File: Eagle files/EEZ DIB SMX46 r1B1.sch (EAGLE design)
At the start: 156 parts, among them IC1 STM32F030C6T6, IC2 74HC1G126DBVT, IC3 M24C32-WMN6P, IC4 LP2985-33DBVR, IC5 74HC2G04GW,125, K1 FTR-C1GA012G-B05, K10 FTR-C1GA012G-B05, K11 FTR-C1GA012G-B05, K12 FTR-C1GA012G-B05, K13 FTR-C1GA012G-B05, K14 FTR-C1GA012G-B05, K15 FTR-C1GA012G-B05, K16 FTR-C1GA012G-B05, K17 FTR-C1GA012G-B05, K18 FTR-C1GA012G-B05, K19 FTR-C1GA012G-B05, K2 FTR-C1GA012G-B05, K20 FTR-C1GA012G-B05, K21 FTR-C1GA012G-B05, K22 FTR-C1GA012G-B05, K23 FTR-C1GA012G-B05, K24 FTR-C1GA012G-B05, K3 FTR-C1GA012G-B05, K4 FTR-C1GA012G-B05, K5 FTR-C1GA012G-B05, K6 FTR-C1GA012G-B05, K7 FTR-C1GA012G-B05, K8 FTR-C1GA012G-B05, K9 FTR-C1GA012G-B05, Q1 2N7002, Q10 2N7002, Q11 2N7002, Q12 2N7002, Q13 2N7002, Q14 2N7002, Q15 2N7002, Q16 2N7002, Q17 2N7002, Q18 2N7002, Q19 2N7002, Q2 2N7002, Q20 2N7002, Q21 2N7002, Q22 2N7002, Q23 2N7002, Q24 2N7002, Q25 2N7002, Q3 2N7002, Q4 2N7002, Q5 2N7002, Q6 2N7002, Q7 2N7002, Q8 2N7002, Q9 2N7002, X1 N.C., X2 77317-104-28LF, X3 691327310016, X4 691327310016

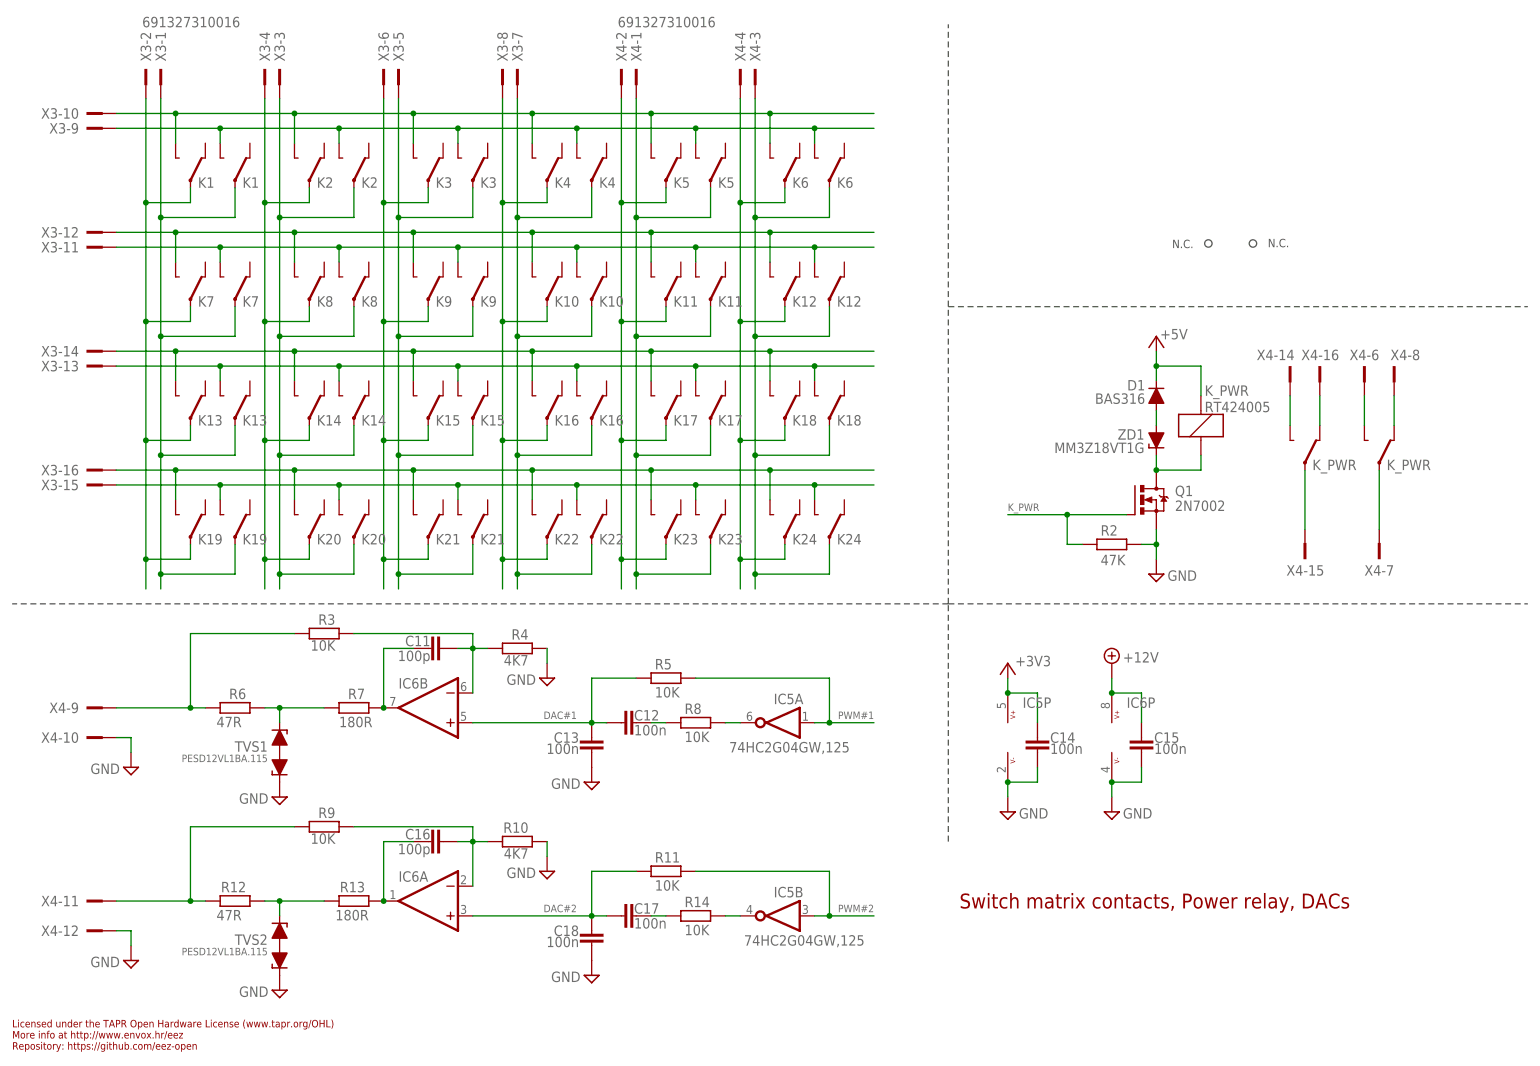
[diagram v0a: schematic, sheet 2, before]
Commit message: UART relocated
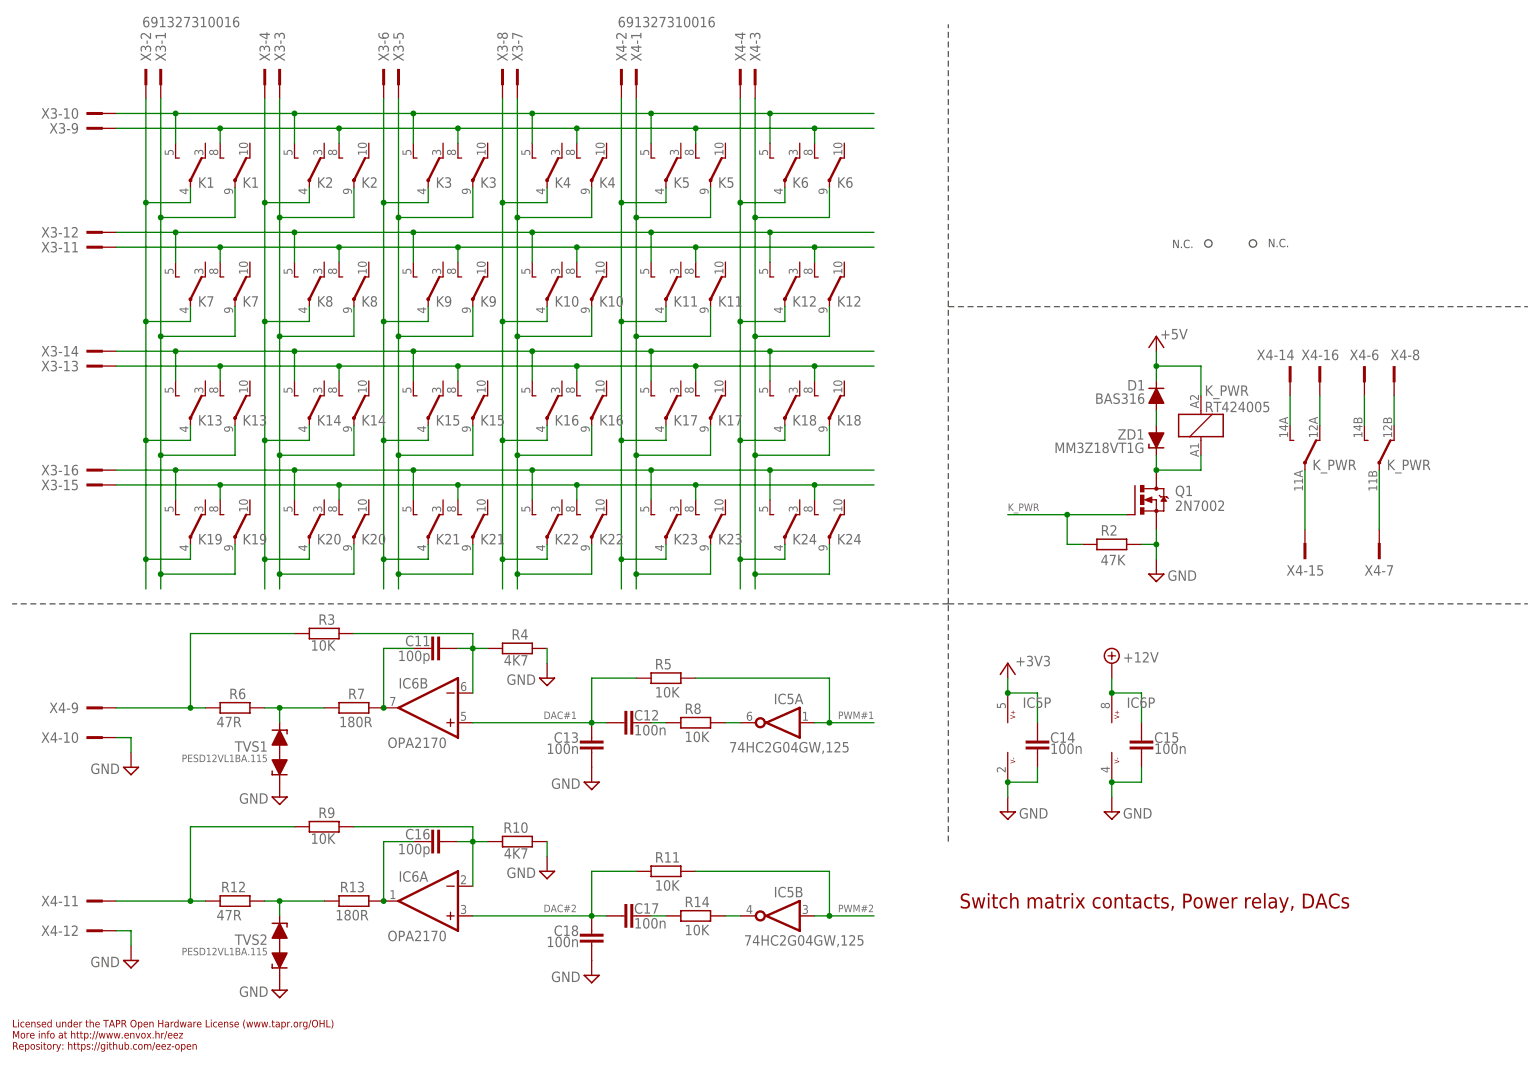
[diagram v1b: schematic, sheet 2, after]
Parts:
- IC6: value (none) -> OPA2170
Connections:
- net K_PWR: now also IC1.PA15; no longer IC1.PA8
- net PWM#1: now also IC1.PA8; no longer IC1.PA10
- net UART_RX: now also IC1.PA10; no longer IC1.PA15
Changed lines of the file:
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@@
 <part name="SUPPLY36" library="supply2" deviceset="GND" device=""/>
 <part name="+3V8" library="supply1" deviceset="+3V3" device=""/>
-<part name="IC6" library="EEZ_Lib1" deviceset="TL072" device="SOIC8"/>
+<part name="IC6" library="EEZ_Lib1" deviceset="TL072" device="SOIC8" value="OPA2170"/>
 <part name="R3" library="rcl" deviceset="R-EU_" device="R0805" value="10K"/>
 <part name="R4" library="rcl" deviceset="R-EU_" device="R0805" value="4K7"/>
@@
 <net name="K_PWR" class="0">
 <segment>
-<pinref part="IC1" gate="G$1" pin="PA8"/>
-<wire x1="241.3" y1="99.06" x2="251.46" y2="99.06" width="0.1524" layer="91"/>
-<label x="243.84" y="99.695" size="1.27" layer="102"/>
+<label x="222.885" y="132.08" size="1.27" layer="102" rot="R90"/>
+<pinref part="IC1" gate="G$1" pin="PA15"/>
+<wire x1="223.52" y1="129.54" x2="223.52" y2="139.7" width="0.1524" layer="91"/>
 </segment>
 </net>
@@
 <net name="PWM#1" class="0">
 <segment>
-<pinref part="IC1" gate="G$1" pin="PA10"/>
-<wire x1="241.3" y1="104.14" x2="251.46" y2="104.14" width="0.1524" layer="91"/>
-<label x="243.84" y="104.775" size="1.27" layer="102"/>
+<label x="243.84" y="99.695" size="1.27" layer="102"/>
+<pinref part="IC1" gate="G$1" pin="PA8"/>
+<wire x1="241.3" y1="99.06" x2="251.46" y2="99.06" width="0.1524" layer="91"/>
 </segment>
 </net>
@@
 <net name="UART_RX" class="0">
 <segment>
-<pinref part="IC1" gate="G$1" pin="PA15"/>
-<wire x1="223.52" y1="129.54" x2="223.52" y2="142.24" width="0.1524" layer="91"/>
-<label x="222.885" y="132.08" size="1.27" layer="102" rot="R90"/>
+<label x="243.84" y="104.775" size="1.27" layer="102"/>
+<wire x1="241.3" y1="104.14" x2="251.46" y2="104.14" width="0.1524" layer="91"/>
+<pinref part="IC1" gate="G$1" pin="PA10"/>
 </segment>
 <segment>
@@
 <segment>
 <pinref part="IC1" gate="G$1" pin="PA14"/>
-<wire x1="226.06" y1="129.54" x2="226.06" y2="142.24" width="0.1524" layer="91"/>
+<wire x1="226.06" y1="129.54" x2="226.06" y2="139.7" width="0.1524" layer="91"/>
 <label x="225.425" y="132.08" size="1.27" layer="102" rot="R90"/>
 </segment>
@@
 <instance part="IC6" gate="B" x="73.66" y="60.96" smashed="yes" rot="R180">
 <attribute name="NAME" x="73.66" y="66.04" size="1.778" layer="95" rot="R180"/>
-<attribute name="VALUE" x="78.74" y="52.07" size="1.778" layer="96" rot="R180"/>
+<attribute name="VALUE" x="76.835" y="55.88" size="1.778" layer="96" rot="R180"/>
 </instance>
 <instance part="C11" gate="G$1" x="73.66" y="71.12" smashed="yes" rot="MR270">
@@
 <instance part="IC6" gate="A" x="73.66" y="27.94" smashed="yes" rot="R180">
 <attribute name="NAME" x="73.66" y="33.02" size="1.778" layer="95" rot="R180"/>
-<attribute name="VALUE" x="71.12" y="33.02" size="1.778" layer="96" rot="R180"/>
+<attribute name="VALUE" x="76.835" y="22.86" size="1.778" layer="96" rot="R180"/>
 </instance>
 <instance part="IC6" gate="P" x="190.5" y="55.88" smashed="yes">

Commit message: debug connector update
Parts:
- X1: value N.C. -> SSW-106-02-S-S; device EEZ_connectors:22-23-2061 -> con-samtec:SSW-106-02-S-S
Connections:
- net GND: now also X1-3.1; no longer X1-3.S
- net SWCLK: now also X1-2.1; no longer X1-2.S
- net SWDIO: now also X1-4.1; no longer X1-4.S
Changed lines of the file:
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@@
 <part name="IC2" library="EEZ_TI" deviceset="74HC1G126" device="DBVT"/>
 <part name="SUPPLY51" library="supply2" deviceset="GND" device=""/>
-<part name="X1" library="EEZ_connectors" deviceset="22-23-2061" device="" value="N.C."/>
 <part name="RN3" library="EEZ_Lib1" deviceset="R_ARRAY4" device="" value="DR1206-47K-4/8"/>
 <part name="RN4" library="EEZ_Lib1" deviceset="R_ARRAY4" device="" value="DR1206-47K-4/8"/>
@@
 <part name="FM2" library="EEZ_Lib1" deviceset="FIDUCIAL" device="_2"/>
 <part name="FM1" library="EEZ_Lib1" deviceset="FIDUCIAL" device="_2"/>
+<part name="X1" library="con-samtec" deviceset="SSW-106-02-S-S" device=""/>
 </parts>
 <sheets>
@@
 <attribute name="VALUE" x="168.275" y="159.385" size="1.778" layer="96" rot="MR0"/>
 </instance>
-<instance part="X1" gate="-2" x="175.26" y="167.64" smashed="yes">
-<attribute name="NAME" x="177.8" y="166.878" size="1.524" layer="95"/>
-</instance>
-<instance part="X1" gate="-3" x="175.26" y="162.56" smashed="yes">
-<attribute name="NAME" x="177.8" y="161.798" size="1.524" layer="95"/>
-</instance>
-<instance part="X1" gate="-4" x="175.26" y="165.1" smashed="yes">
-<attribute name="NAME" x="177.8" y="164.338" size="1.524" layer="95"/>
-</instance>
 <instance part="RN3" gate="-2" x="175.26" y="48.26" smashed="yes" rot="R90">
 <attribute name="NAME" x="175.133" y="50.8" size="1.27" layer="95" rot="R90"/>
@@
 <instance part="FM2" gate="FD" x="137.16" y="5.08" smashed="yes"/>
 <instance part="FM1" gate="FD" x="129.54" y="5.08" smashed="yes"/>
+<instance part="X1" gate="-2" x="177.8" y="167.64" smashed="yes" rot="MR0">
+<attribute name="NAME" x="180.848" y="168.402" size="1.524" layer="95" rot="MR180"/>
+</instance>
+<instance part="X1" gate="-3" x="177.8" y="162.56" smashed="yes" rot="MR0">
+<attribute name="NAME" x="180.848" y="163.322" size="1.524" layer="95" rot="MR180"/>
+</instance>
+<instance part="X1" gate="-4" x="177.8" y="165.1" smashed="yes" rot="MR0">
+<attribute name="NAME" x="180.848" y="165.862" size="1.524" layer="95" rot="MR180"/>
+</instance>
 </instances>
 <busses>
@@
 </segment>
 <segment>
-<pinref part="X1" gate="-3" pin="S"/>
-<wire x1="172.72" y1="162.56" x2="170.18" y2="162.56" width="0.1524" layer="91"/>
 <pinref part="SUPPLY51" gate="GND" pin="GND"/>
+<pinref part="X1" gate="-3" pin="1"/>
+<wire x1="175.26" y1="162.56" x2="170.18" y2="162.56" width="0.1524" layer="91"/>
 </segment>
 <segment>
@@
 </segment>
 <segment>
-<wire x1="152.4" y1="165.1" x2="172.72" y2="165.1" width="0.1524" layer="91"/>
+<wire x1="152.4" y1="165.1" x2="175.26" y2="165.1" width="0.1524" layer="91"/>
 <label x="152.4" y="165.735" size="1.27" layer="102"/>
-<pinref part="X1" gate="-4" pin="S"/>
+<pinref part="X1" gate="-4" pin="1"/>
 </segment>
 </net>
@@
 </segment>
 <segment>
-<wire x1="152.4" y1="167.64" x2="172.72" y2="167.64" width="0.1524" layer="91"/>
+<wire x1="152.4" y1="167.64" x2="175.26" y2="167.64" width="0.1524" layer="91"/>
 <label x="152.4" y="168.275" size="1.27" layer="102"/>
-<pinref part="X1" gate="-2" pin="S"/>
-</segment>
-</net>
+<pinref part="X1" gate="-2" pin="1"/>
+</segment>
+</net>

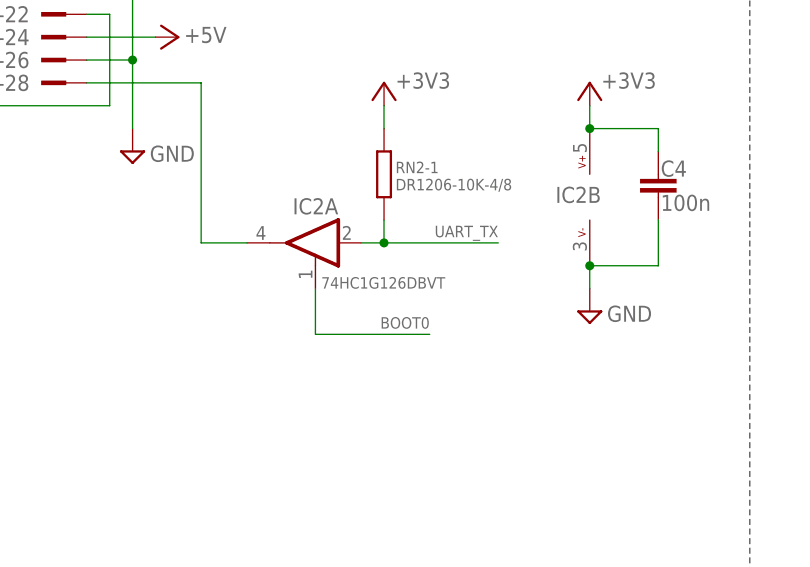
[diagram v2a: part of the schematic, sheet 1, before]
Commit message: IC2 package update
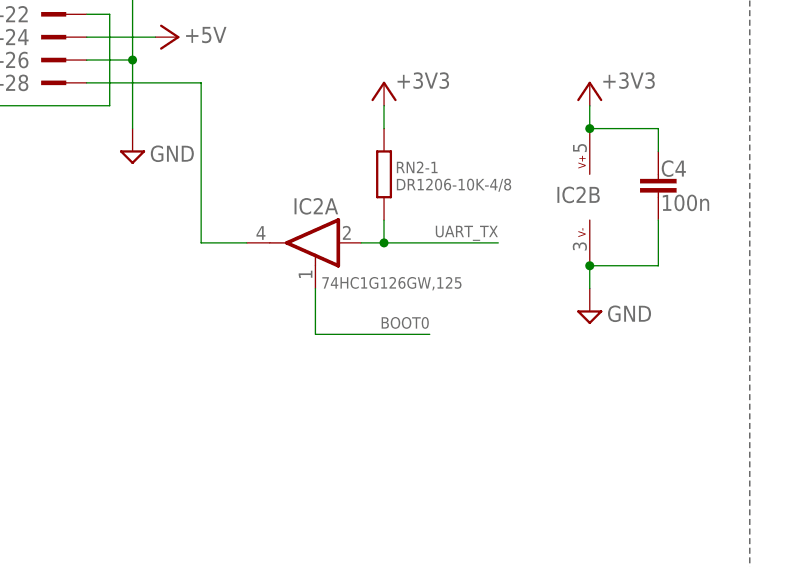
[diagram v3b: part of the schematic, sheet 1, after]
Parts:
- IC2: value 74HC1G126DBVT -> 74HC1G126GW,125; device EEZ_TI:74HC1G126DBVT -> EEZ_Lib1:74HC1G126GW,125
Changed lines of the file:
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@@
 <part name="SUPPLY47" library="supply2" deviceset="GND" device=""/>
 <part name="+3V7" library="supply1" deviceset="+3V3" device=""/>
-<part name="IC2" library="EEZ_TI" deviceset="74HC1G126" device="DBVT"/>
+<part name="IC2" library="EEZ_Lib1" deviceset="74HC1G126" device="GW,125"/>
 <part name="SUPPLY51" library="supply2" deviceset="GND" device=""/>
 <part name="RN3" library="EEZ_Lib1" deviceset="R_ARRAY4" device="" value="DR1206-47K-4/8"/>
